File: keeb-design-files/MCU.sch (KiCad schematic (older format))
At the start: 33 parts, among them J1 Conn_ARM_JTAG_SWD_10, J2 SMA, SW1 RESET, SW70 BOOT0, U1 STM32L452CEUx, U2 nRF24L01P, Y2 Crystal_GND24

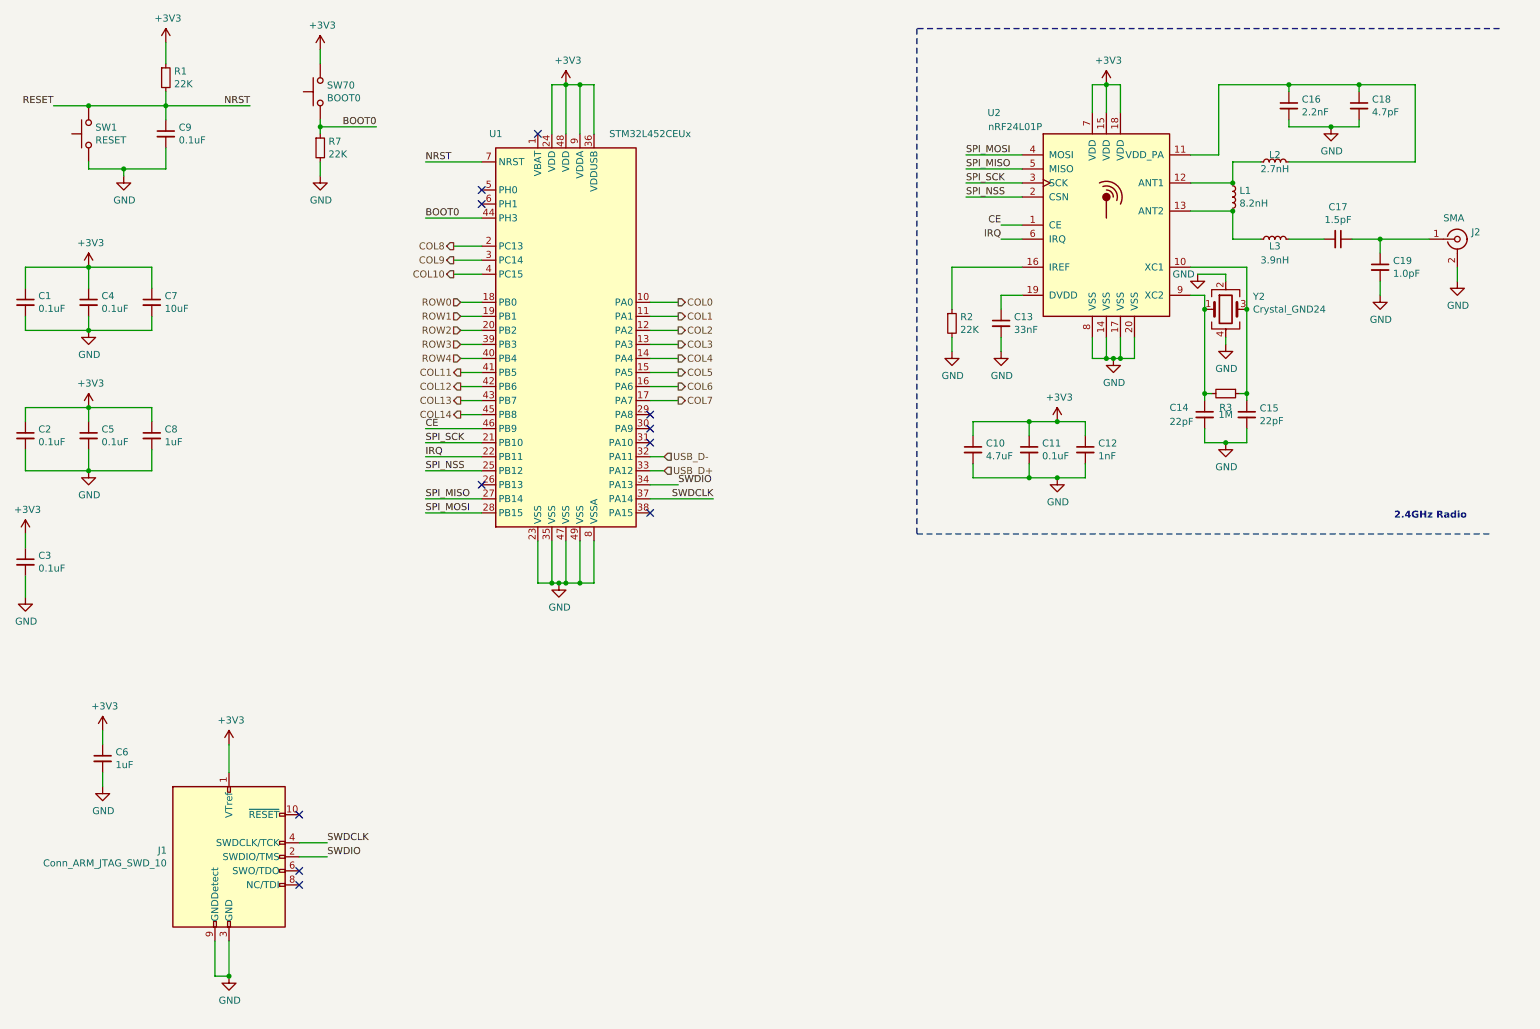
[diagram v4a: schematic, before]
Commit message: Add new connections to MCU for I2C OLED Display and Battery Management
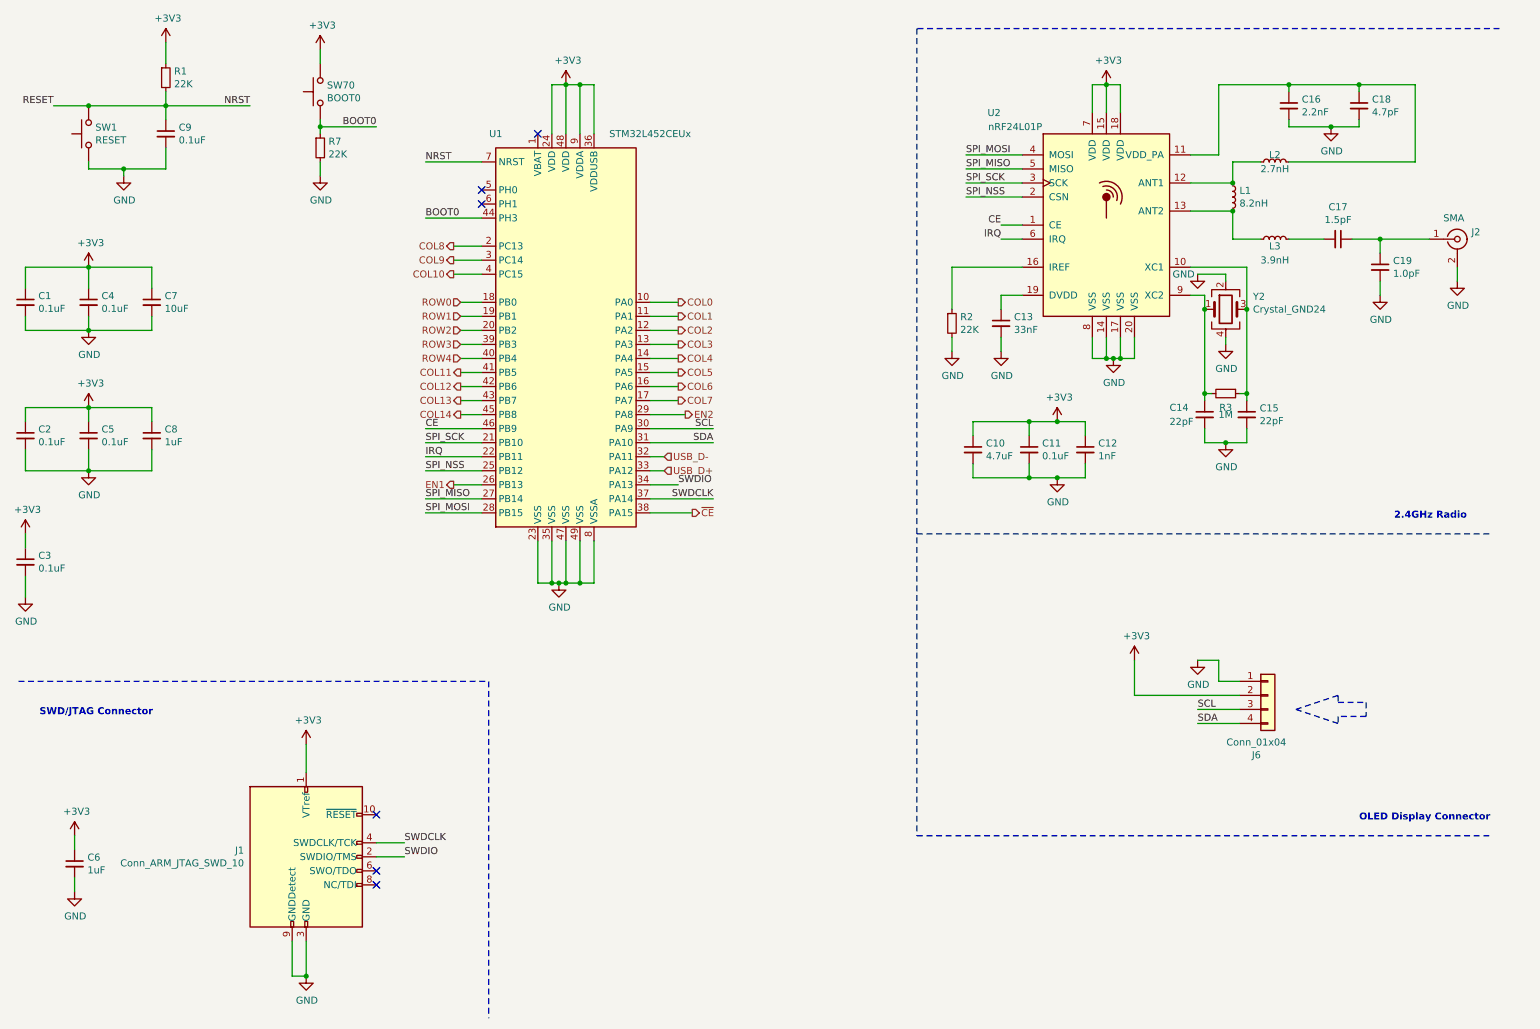
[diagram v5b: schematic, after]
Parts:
- added J6: Conn_01x04, lib_fp:OLED_Display, symbol Connector_Generic:Conn_01x04
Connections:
- net +3V3: now also J6.2 (Pin_2)
- net GND: now also J6.1 (Pin_1)
- net EN1: now reaches U1.26 (PB13)
- net EN2: now reaches U1.29 (PA8)
- net SCL: now reaches U1.30 (PA9)
- net SCL: now also J6.3 (Pin_3)
- net SDA: now reaches U1.31 (PA10)
- net SDA: now also J6.4 (Pin_4)
- net ~CE~: now reaches U1.38 (PA15)
- no-connect marks 11 -> 6
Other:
- note added: "OLED Display Connector"
- note added: "SWD/JTAG Connector"
- moved on the sheet: C6, J1
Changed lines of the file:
@@
 L Connector:Conn_ARM_JTAG_SWD_10 J1
 U 1 1 5EBCB382
-P 2050 6600
-F 0 "J1" H 1607 6646 50  0000 R CNN
-F 1 "Conn_ARM_JTAG_SWD_10" H 1607 6555 50  0000 R CNN
-F 2 "Connector_PinHeader_1.27mm:PinHeader_2x05_P1.27mm_Vertical_SMD" H 2050 6600 50  0001 C CNN
-F 3 "http://infocenter.arm.com/help/topic/com.arm.doc.ddi0314h/DDI0314H_coresight_components_trm.pdf" V 1700 5350 50  0001 C CNN
-	1    2050 6600
+P 2600 6600
+F 0 "J1" H 2157 6646 50  0000 R CNN
+F 1 "Conn_ARM_JTAG_SWD_10" H 2157 6555 50  0000 R CNN
+F 2 "Connector_PinHeader_1.27mm:PinHeader_2x05_P1.27mm_Vertical_SMD" H 2600 6600 50  0001 C CNN
+F 3 "http://infocenter.arm.com/help/topic/com.arm.doc.ddi0314h/DDI0314H_coresight_components_trm.pdf" V 2250 5350 50  0001 C CNN
+	1    2600 6600
 	1    0    0    -1
 $EndComp
@@
 L power:+3V3 #PWR0119
 U 1 1 5EACEE85
-P 2050 5800
-F 0 "#PWR0119" H 2050 5650 50  0001 C CNN
-F 1 "+3V3" H 2065 5973 50  0000 C CNN
-F 2 "" H 2050 5800 50  0001 C CNN
-F 3 "" H 2050 5800 50  0001 C CNN
-	1    2050 5800
-	1    0    0    -1
-$EndComp
-Wire Wire Line
-	2050 5800 2050 6000
+P 2600 5800
+F 0 "#PWR0119" H 2600 5650 50  0001 C CNN
+F 1 "+3V3" H 2615 5973 50  0000 C CNN
+F 2 "" H 2600 5800 50  0001 C CNN
+F 3 "" H 2600 5800 50  0001 C CNN
+	1    2600 5800
+	1    0    0    -1
+$EndComp
+Wire Wire Line
+	2600 5800 2600 6000
 $Comp
 L Device:C_Small C6
 U 1 1 5EAD895B
-P 1150 5900
-F 0 "C6" H 1242 5946 50  0000 L CNN
-F 1 "1uF" H 1242 5855 50  0000 L CNN
-F 2 "Capacitor_SMD:C_0402_1005Metric" H 1150 5900 50  0001 C CNN
-F 3 "~" H 1150 5900 50  0001 C CNN
-F 4 "C52923" H 1150 5900 50  0001 C CNN "LCSC Part Number"
-	1    1150 5900
+P 950 6650
+F 0 "C6" H 1042 6696 50  0000 L CNN
+F 1 "1uF" H 1042 6605 50  0000 L CNN
+F 2 "Capacitor_SMD:C_0402_1005Metric" H 950 6650 50  0001 C CNN
+F 3 "~" H 950 6650 50  0001 C CNN
+F 4 "C52923" H 950 6650 50  0001 C CNN "LCSC Part Number"
+	1    950  6650
 	1    0    0    -1
 $EndComp
@@
 L power:+3V3 #PWR0120
 U 1 1 5EAD8D53
-P 1150 5700
-F 0 "#PWR0120" H 1150 5550 50  0001 C CNN
-F 1 "+3V3" H 1165 5873 50  0000 C CNN
-F 2 "" H 1150 5700 50  0001 C CNN
-F 3 "" H 1150 5700 50  0001 C CNN
-	1    1150 5700
+P 950 6450
+F 0 "#PWR0120" H 950 6300 50  0001 C CNN
+F 1 "+3V3" H 965 6623 50  0000 C CNN
+F 2 "" H 950 6450 50  0001 C CNN
+F 3 "" H 950 6450 50  0001 C CNN
+	1    950  6450
 	1    0    0    -1
 $EndComp
@@
 L power:GND #PWR0121
 U 1 1 5EAD98B4
-P 1150 6100
-F 0 "#PWR0121" H 1150 5850 50  0001 C CNN
-F 1 "GND" H 1155 5927 50  0000 C CNN
-F 2 "" H 1150 6100 50  0001 C CNN
-F 3 "" H 1150 6100 50  0001 C CNN
-	1    1150 6100
-	1    0    0    -1
-$EndComp
-Wire Wire Line
-	1150 6100 1150 6000
-Wire Wire Line
-	1150 5800 1150 5700
+P 950 6850
+F 0 "#PWR0121" H 950 6600 50  0001 C CNN
+F 1 "GND" H 955 6677 50  0000 C CNN
+F 2 "" H 950 6850 50  0001 C CNN
+F 3 "" H 950 6850 50  0001 C CNN
+	1    950  6850
+	1    0    0    -1
+$EndComp
+Wire Wire Line
+	950  6850 950  6750
+Wire Wire Line
+	950  6550 950  6450
 $Comp
 L power:GND #PWR0122
 U 1 1 5EAE8DF9
-P 2050 7450
-F 0 "#PWR0122" H 2050 7200 50  0001 C CNN
-F 1 "GND" H 2055 7277 50  0000 C CNN
-F 2 "" H 2050 7450 50  0001 C CNN
-F 3 "" H 2050 7450 50  0001 C CNN
-	1    2050 7450
-	1    0    0    -1
-$EndComp
-Wire Wire Line
-	2050 7450 2050 7200
-Wire Wire Line
-	1950 7200 1950 7450
-Wire Wire Line
-	1950 7450 2050 7450
-Connection ~ 2050 7450
-Text Label 2750 6500 0    50   ~ 0
+P 2600 7450
+F 0 "#PWR0122" H 2600 7200 50  0001 C CNN
+F 1 "GND" H 2605 7277 50  0000 C CNN
+F 2 "" H 2600 7450 50  0001 C CNN
+F 3 "" H 2600 7450 50  0001 C CNN
+	1    2600 7450
+	1    0    0    -1
+$EndComp
+Wire Wire Line
+	2600 7450 2600 7200
+Wire Wire Line
+	2500 7200 2500 7450
+Wire Wire Line
+	2500 7450 2600 7450
+Connection ~ 2600 7450
+Text Label 3300 6500 0    50   ~ 0
 SWDCLK
-Text Label 2750 6600 0    50   ~ 0
+Text Label 3300 6600 0    50   ~ 0
 SWDIO
 Wire Wire Line
-	2750 6500 2550 6500
-Wire Wire Line
-	2750 6600 2550 6600
+	3300 6500 3100 6500
+Wire Wire Line
+	3300 6600 3100 6600
 Text Label 5250 3950 0    50   ~ 0
 SWDIO
@@
 	11100 700  6950 700
 Wire Notes Line width 20
-	6950 700  6950 4300
-Wire Notes Line width 20
 	6950 4300 11050 4300
 Text Notes 10350 4200 0    50   ~ 10
@@
 Text Label 3450 4050 0    50   ~ 0
 SPI_MISO
-NoConn ~ 2550 6300
-NoConn ~ 2550 6700
-NoConn ~ 2550 6800
+NoConn ~ 3100 6300
+NoConn ~ 3100 6700
+NoConn ~ 3100 6800
 Text Label 3450 2050 0    50   ~ 0
 BOOT0
@@
 NoConn ~ 3850 1850
 NoConn ~ 3850 1950
-NoConn ~ 3850 3950
-NoConn ~ 5050 4150
-NoConn ~ 5050 3650
-NoConn ~ 5050 3550
-NoConn ~ 5050 3450
+Wire Wire Line
+	5350 4150 5050 4150
+Text HLabel 5350 4150 2    50   Output ~ 0
+~CE~
+Text HLabel 3650 3950 0    50   Output ~ 0
+EN1
+Text HLabel 5300 3450 2    50   Output ~ 0
+EN2
+$Comp
+L Connector_Generic:Conn_01x04 J6
+U 1 1 5EC1B74C
+P 9450 5450
+F 0 "J6" H 9368 5025 50  0000 C CNN
+F 1 "Conn_01x04" H 9368 5116 50  0000 C CNN
+F 2 "lib_fp:OLED_Display" H 9450 5450 50  0001 C CNN
+F 3 "~" H 9450 5450 50  0001 C CNN
+	1    9450 5450
+	1    0    0    -1
+$EndComp
+$Comp
+L power:GND #PWR0147
+U 1 1 5EC1C40E
+P 8950 5200
+F 0 "#PWR0147" H 8950 4950 50  0001 C CNN
+F 1 "GND" H 8955 5027 50  0000 C CNN
+F 2 "" H 8950 5200 50  0001 C CNN
+F 3 "" H 8950 5200 50  0001 C CNN
+	1    8950 5200
+	1    0    0    -1
+$EndComp
+Wire Wire Line
+	8950 5200 9100 5200
+$Comp
+L power:+3V3 #PWR0148
+U 1 1 5EC263E6
+P 8500 5200
+F 0 "#PWR0148" H 8500 5050 50  0001 C CNN
+F 1 "+3V3" H 8515 5373 50  0000 C CNN
+F 2 "" H 8500 5200 50  0001 C CNN
+F 3 "" H 8500 5200 50  0001 C CNN
+	1    8500 5200
+	1    0    0    -1
+$EndComp
+Wire Wire Line
+	8500 5200 8500 5450
+Wire Wire Line
+	8500 5450 9250 5450
+Text Label 8950 5550 0    50   ~ 0
+SCL
+Wire Wire Line
+	8950 5550 9250 5550
+Text Label 8950 5650 0    50   ~ 0
+SDA
+Wire Wire Line
+	8950 5650 9250 5650
+Wire Wire Line
+	9100 5200 9100 5350
+Wire Wire Line
+	9100 5350 9250 5350
+Text Label 5500 3550 2    50   ~ 0
+SCL
+Wire Wire Line
+	5050 3550 5500 3550
+Text Label 5500 3650 2    50   ~ 0
+SDA
+Wire Wire Line
+	5050 3650 5500 3650
+Wire Wire Line
+	5050 3450 5300 3450
+Wire Wire Line
+	3650 3950 3850 3950
+Wire Notes Line
+	9650 5550 9950 5450
+Wire Notes Line
+	9950 5650 9650 5550
+Wire Notes Line
+	9950 5450 9950 5500
+Wire Notes Line
+	9950 5500 10150 5500
+Wire Notes Line
+	10150 5500 10150 5600
+Wire Notes Line
+	10150 5600 9950 5600
+Wire Notes Line
+	9950 5600 9950 5650
+Text Notes 10100 6350 0    50   ~ 10
+OLED Display Connector
+Wire Notes Line width 20
+	6950 6450 11050 6450
+Wire Notes Line width 20
+	6950 700  6950 6450
+Wire Notes Line width 20
+	550  5350 3900 5350
+Wire Notes Line width 20
+	3900 5350 3900 7750
+Text Notes 700  5600 0    50   ~ 10
+SWD/JTAG Connector
 $EndSCHEMATC
